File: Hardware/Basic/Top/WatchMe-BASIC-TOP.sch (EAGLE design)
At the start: 65 parts, among them SW1 SWITCH.MOM, SW2 SWITCH.MOM, U2 NRF52832_MODULE_MDBT42, U4 PCF8523, U5 FT231XS

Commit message: continuin top board work
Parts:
- removed C10, C11: 300p, LinnesLab-Passives:CAPACITOR0603
- removed R15: 100k, LinnesLab-Passives:RESISTOR0603
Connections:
- net 3.3V: no longer R15.2
- net GND: no longer C10.2, C11.2, R15.1, SW1.4, SW2.4
- net P0.09/NFC1: no longer C11.1
- net P0.10/NFC2: no longer C10.1
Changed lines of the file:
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@@
 <part name="GND15" library="LinnesLab-Symbols" deviceset="GND" device=""/>
 <part name="GND16" library="LinnesLab-Symbols" deviceset="GND" device=""/>
-<part name="GND17" library="LinnesLab-Symbols" deviceset="GND" device=""/>
-<part name="GND18" library="LinnesLab-Symbols" deviceset="GND" device=""/>
 <part name="GND19" library="LinnesLab-Symbols" deviceset="GND" device=""/>
 <part name="GND20" library="LinnesLab-Symbols" deviceset="GND" device=""/>
@@
 <part name="C8" library="LinnesLab-Passives" deviceset="CAPACITOR" device="0603" package3d_urn="urn:adsk.eagle:package:15661989/2"/>
 <part name="C9" library="LinnesLab-Passives" deviceset="CAPACITOR" device="0603" package3d_urn="urn:adsk.eagle:package:15661989/2"/>
-<part name="C10" library="LinnesLab-Passives" deviceset="CAPACITOR" device="0603" package3d_urn="urn:adsk.eagle:package:15661989/2" value="300p"/>
-<part name="C11" library="LinnesLab-Passives" deviceset="CAPACITOR" device="0603" package3d_urn="urn:adsk.eagle:package:15661989/2" value="300p"/>
 <part name="C12" library="LinnesLab-Passives" deviceset="CAPACITOR" device="0805" package3d_urn="urn:adsk.eagle:package:15662010/2" value="10u"/>
 <part name="L2" library="LinnesLab-Passives" deviceset="INDUCTOR" device="0603" override_package3d_urn="urn:adsk.eagle:package:18592195/2" override_package_urn="urn:adsk.eagle:footprint:18592196/1" value="10u"/>
@@
 <part name="SUPPLY16" library="LinnesLab-Symbols" deviceset="VLIPO" device=""/>
 <part name="GND43" library="LinnesLab-Symbols" deviceset="GND" device=""/>
-<part name="R15" library="LinnesLab-Passives" deviceset="RESISTOR" device="0603" package3d_urn="urn:adsk.eagle:package:15661944/2" value="100k"/>
-<part name="GND44" library="LinnesLab-Symbols" deviceset="GND" device=""/>
 <part name="SUPPLY17" library="LinnesLab-Symbols" deviceset="VIN" device=""/>
 <part name="GND4" library="LinnesLab-Symbols" deviceset="GND" device=""/>
@@
 <attribute name="VALUE" x="-33.02" y="190.246" size="1.778" layer="96" align="top-center"/>
 </instance>
-<instance part="GND17" gate="G$1" x="-30.48" y="160.02" smashed="yes">
-<attribute name="VALUE" x="-30.48" y="159.766" size="1.778" layer="96" align="top-center"/>
-</instance>
-<instance part="GND18" gate="G$1" x="-43.18" y="160.02" smashed="yes">
-<attribute name="VALUE" x="-43.18" y="159.766" size="1.778" layer="96" align="top-center"/>
-</instance>
 <instance part="GND19" gate="G$1" x="-53.34" y="160.02" smashed="yes">
 <attribute name="VALUE" x="-53.34" y="159.766" size="1.778" layer="96" align="top-center"/>
@@
 <attribute name="VALUE" x="-51.816" y="165.481" size="1.778" layer="96"/>
 </instance>
-<instance part="C10" gate="G$1" x="-30.48" y="167.64" smashed="yes">
-<attribute name="NAME" x="-28.956" y="170.561" size="1.778" layer="95"/>
-<attribute name="VALUE" x="-28.956" y="165.481" size="1.778" layer="96"/>
-</instance>
-<instance part="C11" gate="G$1" x="-43.18" y="167.64" smashed="yes">
-<attribute name="NAME" x="-41.656" y="170.561" size="1.778" layer="95"/>
-<attribute name="VALUE" x="-41.656" y="165.481" size="1.778" layer="96"/>
-</instance>
 <instance part="C12" gate="G$1" x="-73.66" y="203.2" smashed="yes" rot="R180">
 <attribute name="NAME" x="-75.184" y="200.279" size="1.778" layer="95" rot="R180"/>
@@
 <instance part="GND43" gate="G$1" x="-30.48" y="-104.14" smashed="yes">
 <attribute name="VALUE" x="-30.48" y="-104.394" size="1.778" layer="96" align="top-center"/>
-</instance>
-<instance part="R15" gate="G$1" x="-17.78" y="-68.58" smashed="yes" rot="R90">
-<attribute name="NAME" x="-19.2786" y="-72.39" size="1.778" layer="95" rot="R90"/>
-<attribute name="VALUE" x="-14.478" y="-72.39" size="1.778" layer="96" rot="R90"/>
-</instance>
-<instance part="GND44" gate="G$1" x="-17.78" y="-78.74" smashed="yes">
-<attribute name="VALUE" x="-17.78" y="-78.994" size="1.778" layer="96" align="top-center"/>
 </instance>
 <instance part="SUPPLY17" gate="G$1" x="-76.2" y="-58.42" smashed="yes">
@@
 <pinref part="GND20" gate="G$1" pin="GND"/>
 <pinref part="C8" gate="G$1" pin="1"/>
-</segment>
-<segment>
-<pinref part="C11" gate="G$1" pin="2"/>
-<pinref part="GND18" gate="G$1" pin="GND"/>
-<wire x1="-43.18" y1="162.56" x2="-43.18" y2="165.1" width="0.1524" layer="91"/>
-</segment>
-<segment>
-<pinref part="C10" gate="G$1" pin="2"/>
-<pinref part="GND17" gate="G$1" pin="GND"/>
-<wire x1="-30.48" y1="162.56" x2="-30.48" y2="165.1" width="0.1524" layer="91"/>
 </segment>
 <segment>
@@
 </segment>
 <segment>
-<pinref part="R15" gate="G$1" pin="1"/>
-<pinref part="GND44" gate="G$1" pin="GND"/>
-<wire x1="-17.78" y1="-76.2" x2="-17.78" y2="-73.66" width="0.1524" layer="91"/>
-</segment>
-<segment>
 <wire x1="238.76" y1="-81.28" x2="236.22" y2="-81.28" width="0.1524" layer="91"/>
 <wire x1="236.22" y1="-83.82" x2="236.22" y2="-81.28" width="0.1524" layer="91"/>
@@
 <pinref part="SW1" gate="G$1" pin="3"/>
 <wire x1="261.62" y1="15.24" x2="264.16" y2="15.24" width="0.1524" layer="91"/>
-<wire x1="264.16" y1="15.24" x2="264.16" y2="12.7" width="0.1524" layer="91"/>
-<pinref part="SW1" gate="G$1" pin="4"/>
-<wire x1="264.16" y1="7.62" x2="264.16" y2="12.7" width="0.1524" layer="91"/>
-<wire x1="264.16" y1="12.7" x2="261.62" y2="12.7" width="0.1524" layer="91"/>
+<wire x1="264.16" y1="7.62" x2="264.16" y2="15.24" width="0.1524" layer="91"/>
 <pinref part="GND1" gate="G$1" pin="GND"/>
 </segment>
@@
 <pinref part="SW2" gate="G$1" pin="3"/>
 <wire x1="294.64" y1="15.24" x2="297.18" y2="15.24" width="0.1524" layer="91"/>
-<wire x1="297.18" y1="15.24" x2="297.18" y2="12.7" width="0.1524" layer="91"/>
-<pinref part="SW2" gate="G$1" pin="4"/>
-<wire x1="297.18" y1="7.62" x2="297.18" y2="12.7" width="0.1524" layer="91"/>
-<wire x1="297.18" y1="12.7" x2="294.64" y2="12.7" width="0.1524" layer="91"/>
+<wire x1="297.18" y1="7.62" x2="297.18" y2="15.24" width="0.1524" layer="91"/>
 <pinref part="GND3" gate="G$1" pin="GND"/>
 </segment>
@@
 <wire x1="-27.94" y1="-58.42" x2="-27.94" y2="-60.96" width="0.1524" layer="91"/>
 <junction x="-27.94" y="-60.96"/>
-<wire x1="-27.94" y1="-60.96" x2="-17.78" y2="-60.96" width="0.1524" layer="91"/>
-<pinref part="R15" gate="G$1" pin="2"/>
-<wire x1="-17.78" y1="-60.96" x2="-17.78" y2="-63.5" width="0.1524" layer="91"/>
 </segment>
 <segment>
@@
 <segment>
 <wire x1="-38.1" y1="195.58" x2="-38.1" y2="175.26" width="0.1524" layer="91"/>
-<wire x1="-43.18" y1="175.26" x2="-38.1" y2="175.26" width="0.1524" layer="91"/>
-<wire x1="-43.18" y1="175.26" x2="-43.18" y2="172.72" width="0.1524" layer="91"/>
-<pinref part="C11" gate="G$1" pin="1"/>
 <pinref part="U2" gate="G$1" pin="P0.09"/>
 <label x="-38.1" y="177.8" size="1.27" layer="95" rot="R180" xref="yes"/>
@@
 <segment>
 <wire x1="-35.56" y1="195.58" x2="-35.56" y2="175.26" width="0.1524" layer="91"/>
-<wire x1="-35.56" y1="175.26" x2="-30.48" y2="175.26" width="0.1524" layer="91"/>
-<wire x1="-30.48" y1="175.26" x2="-30.48" y2="172.72" width="0.1524" layer="91"/>
-<pinref part="C10" gate="G$1" pin="1"/>
 <pinref part="U2" gate="G$1" pin="P0.10"/>
 <label x="-35.56" y="177.8" size="1.27" layer="95" xref="yes"/>

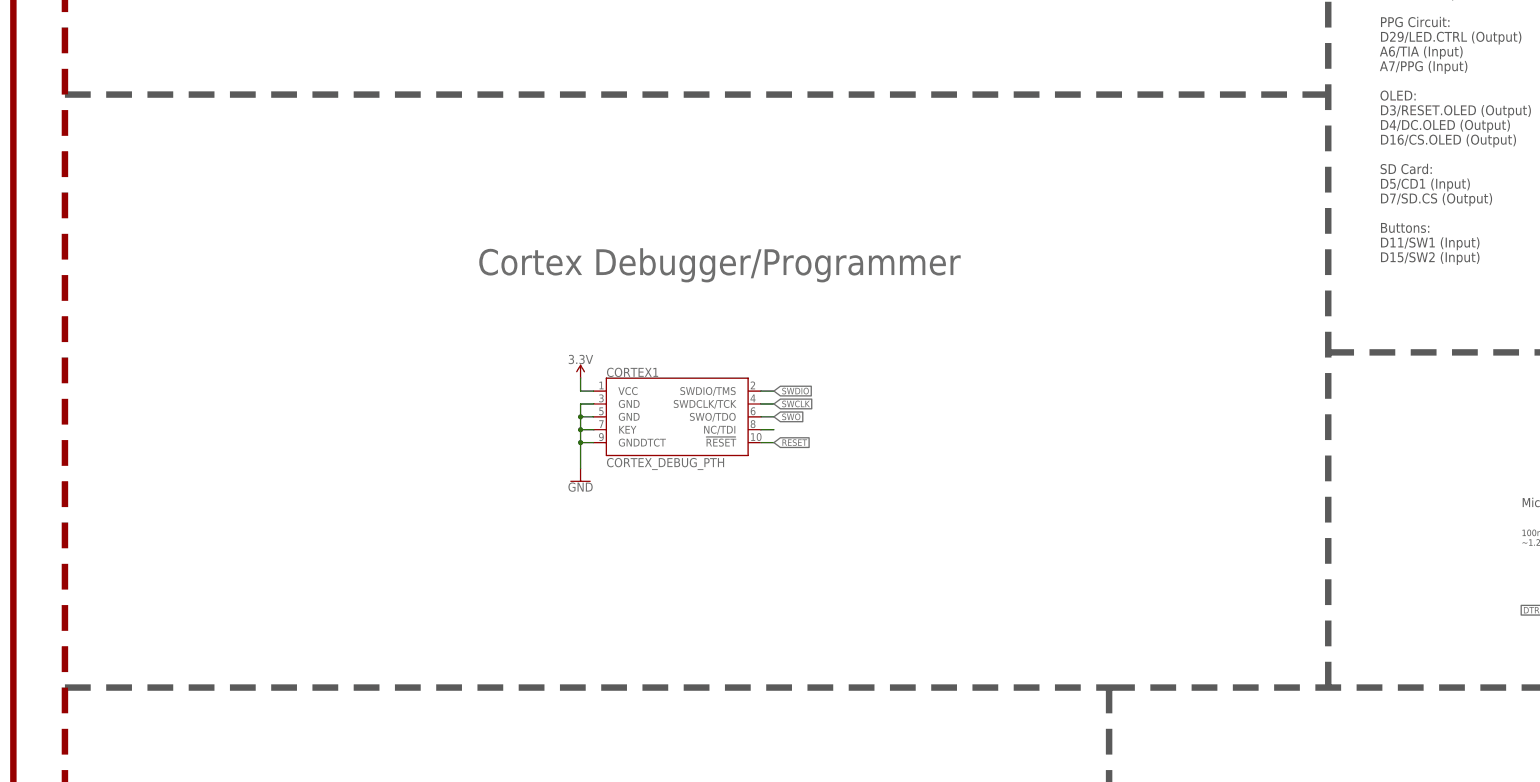
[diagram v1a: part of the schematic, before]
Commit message: Added LSM6DS3 sensor
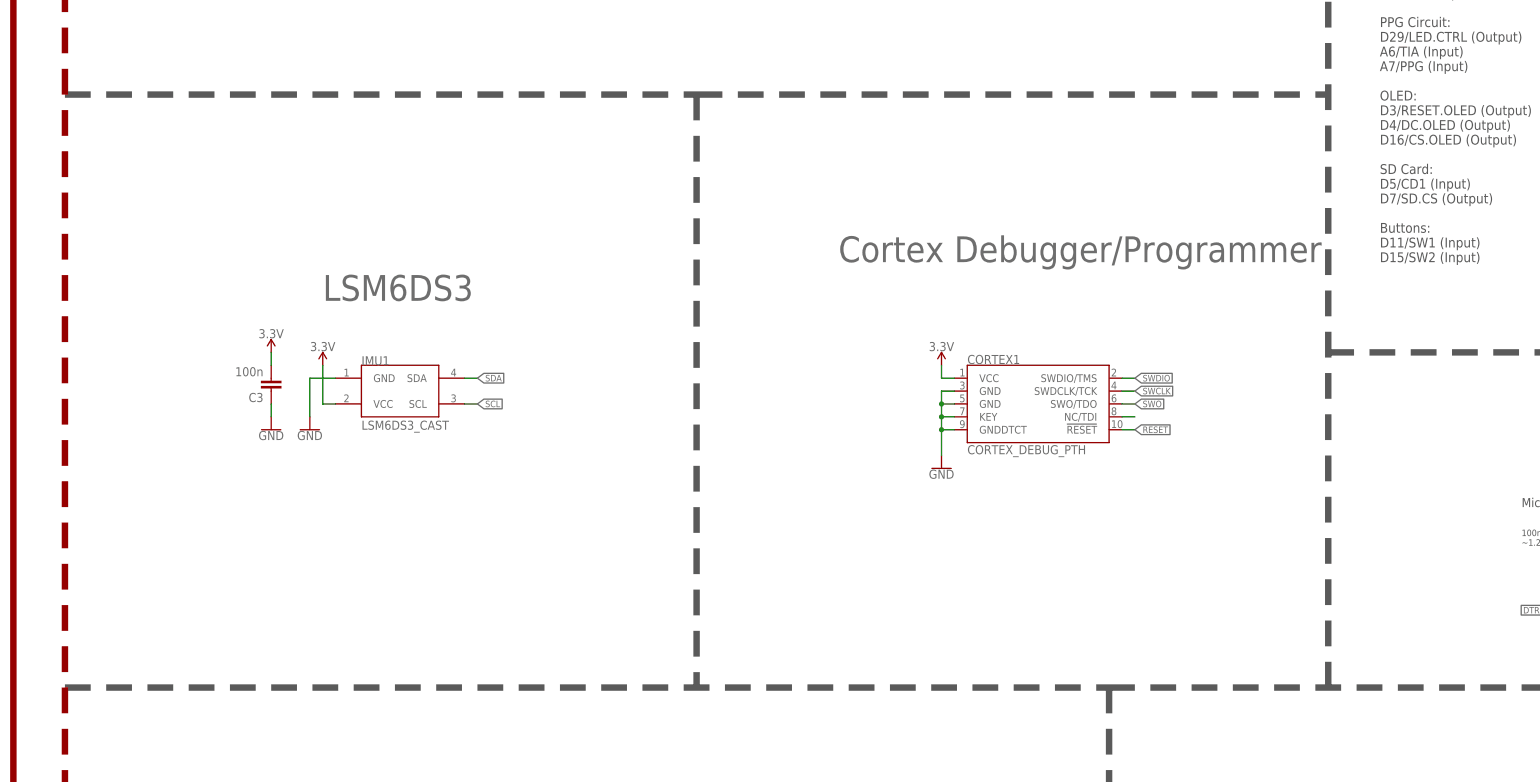
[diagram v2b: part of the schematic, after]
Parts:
- added C3: 100n, LinnesLab-Passives:CAPACITOR0603
- added IMU1: LSM6DS3_CAST, LinnesLab-Sensors:LSM6DS3_CAST
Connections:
- net 3.3V: now also C3.2, IMU1.VCC
- net GND: now also C3.1, IMU1.GND
- net SCL: now also IMU1.SCL
- net SDA: now also IMU1.SDA
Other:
- note added: "LSM6DS3"
- moved on the sheet: CORTEX1

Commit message: removed LSM6DS3 sensor - already on bottom board
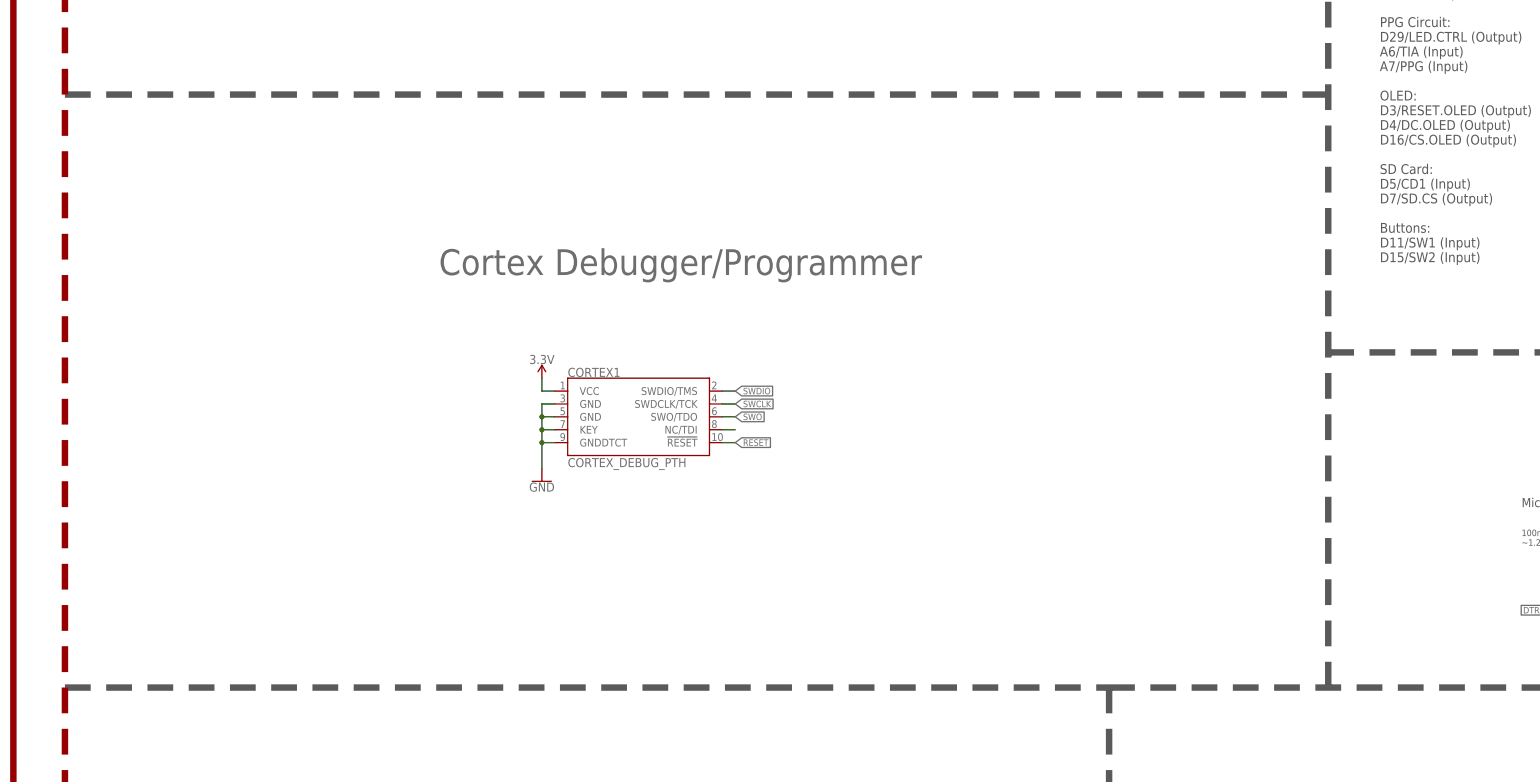
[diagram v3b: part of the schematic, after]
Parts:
- removed C3: 100n, LinnesLab-Passives:CAPACITOR0603
- removed IMU1: LSM6DS3_CAST, LinnesLab-Sensors:LSM6DS3_CAST
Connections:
- net 3.3V: no longer C3.2, IMU1.VCC
- net GND: no longer C3.1, IMU1.GND
- net SCL: no longer IMU1.SCL
- net SDA: no longer IMU1.SDA
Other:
- note removed: "LSM6DS3"
- moved on the sheet: CORTEX1
